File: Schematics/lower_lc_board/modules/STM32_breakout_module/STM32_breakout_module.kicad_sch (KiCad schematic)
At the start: 44 parts, among them J2 SWD_CONN, J3 USB_C_CONN, SW1 SW_STM_RESET, SW2 SW_STM_BOOT_MODE, U5 STM32F103CBT6, U6 W25Q128JVS, U7 ISO1044BDR, U8 CP2102N-Axx-xQFN28, Y1 X322516MMB4SI

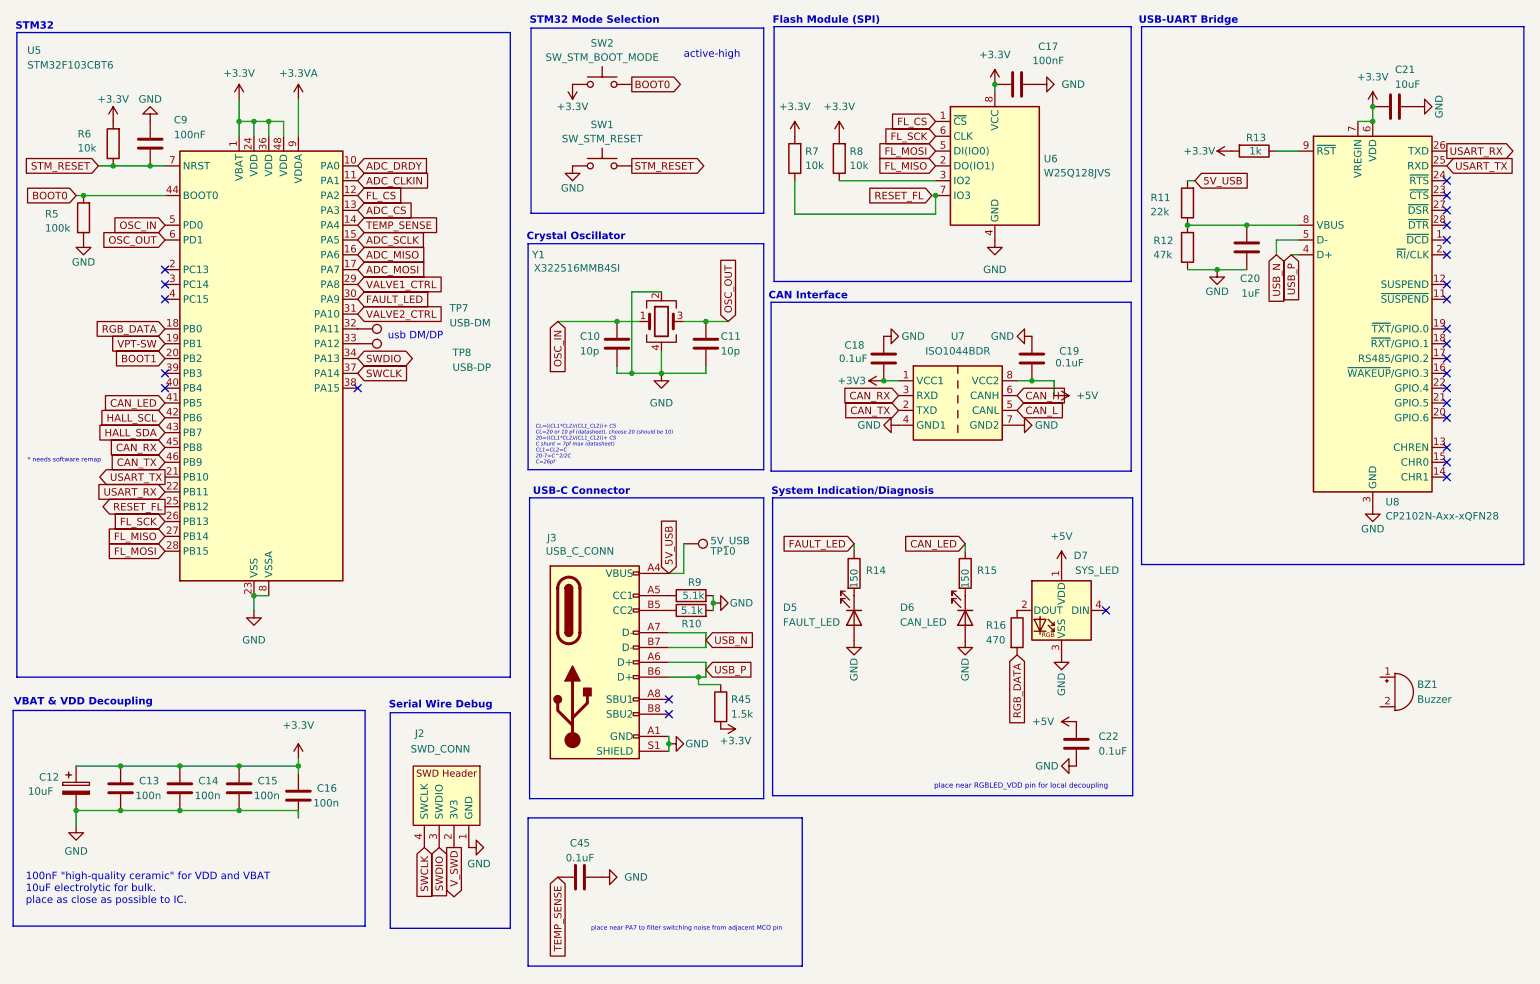
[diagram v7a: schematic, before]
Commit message: add buzzer circuitry, some layout work
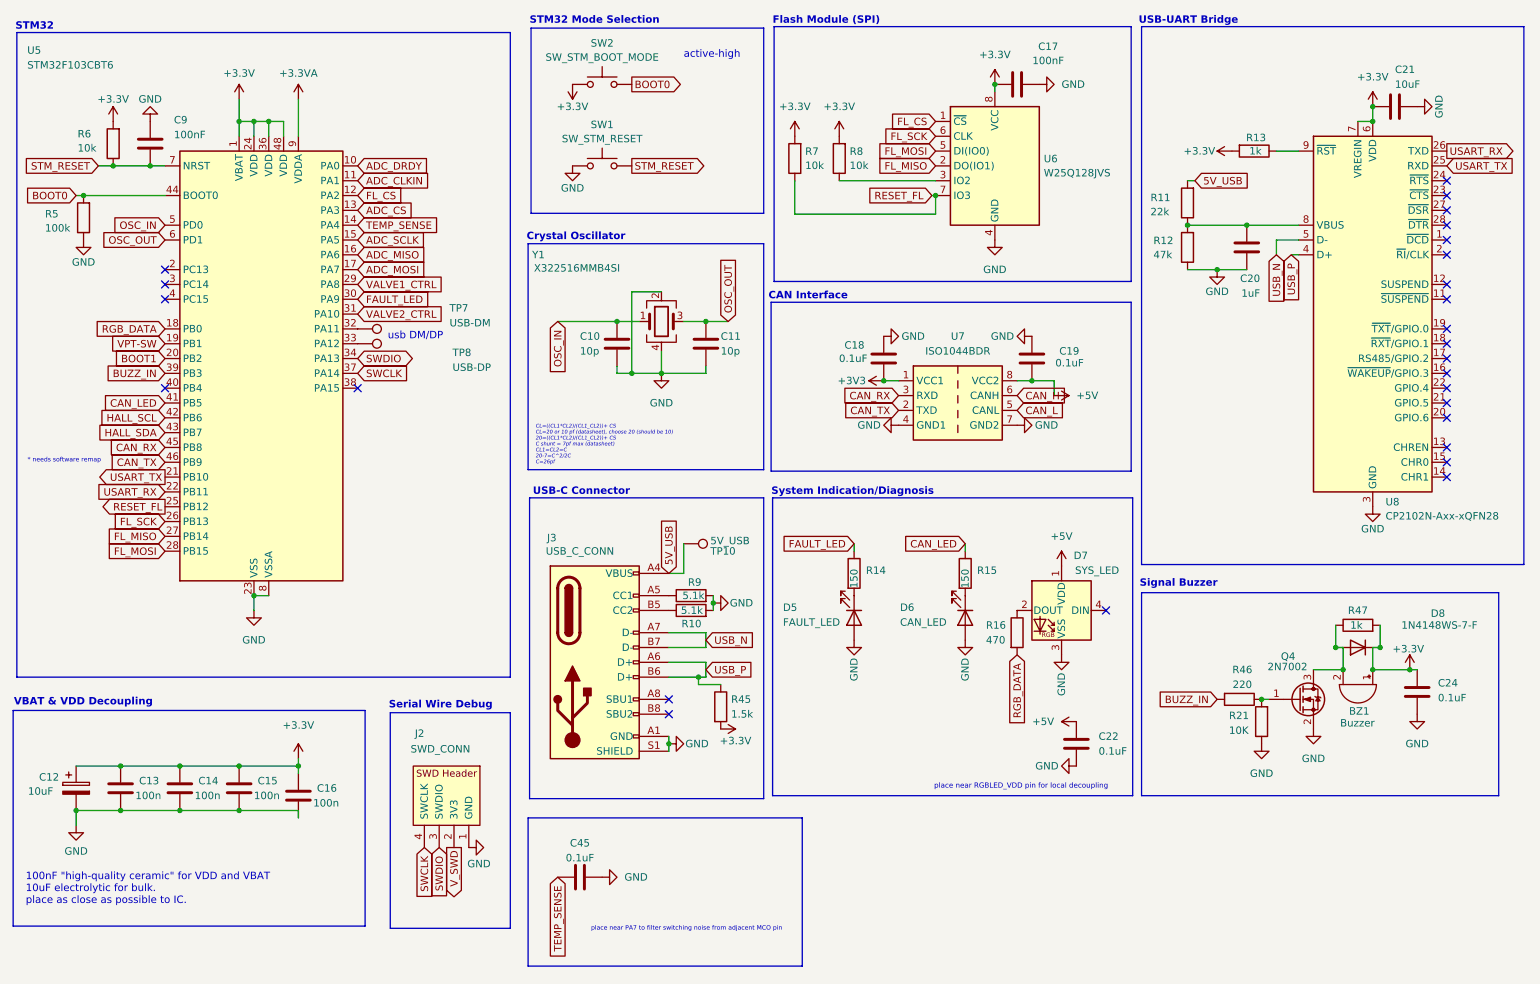
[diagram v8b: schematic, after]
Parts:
- added C24: 0.1uF, Capacitor_SMD:C_0603_1608Metric, symbol Device:C
- added D8: 1N4148WS-7-F, Diode_SMD:D_SOD-323, symbol Diode:1N4148WS
- added Q4: 2N7002, Package_TO_SOT_SMD:SOT-23, symbol Transistor_FET:2N7002
- added R21: 10K, Resistor_SMD:R_0402_1005Metric, symbol Device:R
- added R46: 220, Resistor_SMD:R_0402_1005Metric, symbol Device:R
- added R47: 1k, Resistor_SMD:R_0402_1005Metric, symbol Device:R
- BZ1: footprint (none) -> Buzzer_Beeper:Buzzer_TDK_PS1240P02BT_D12.2mm_H6.5mm
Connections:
- net +3.3V: now also BZ1.1 (+), C24.1, D8.1 (K), R47.2
- net GND: now also C24.2, Q4.2 (S), R21.1
- net BUZZ_IN: now reaches U5.39 (PB3)
- net BUZZ_IN: now also R46.2
- net at BZ1.2 (-): now also D8.2 (A), Q4.3 (D), R47.1
- new net: Q4.1 (G), R21.2, R46.1
- no-connect marks 27 -> 26
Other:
- note added: "Signal Buzzer"
- moved on the sheet: BZ1
